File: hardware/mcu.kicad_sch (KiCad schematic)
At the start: 25 parts, among them SW1 SW_Push, SW4 SW_Push, U1 STM32L072RBTx

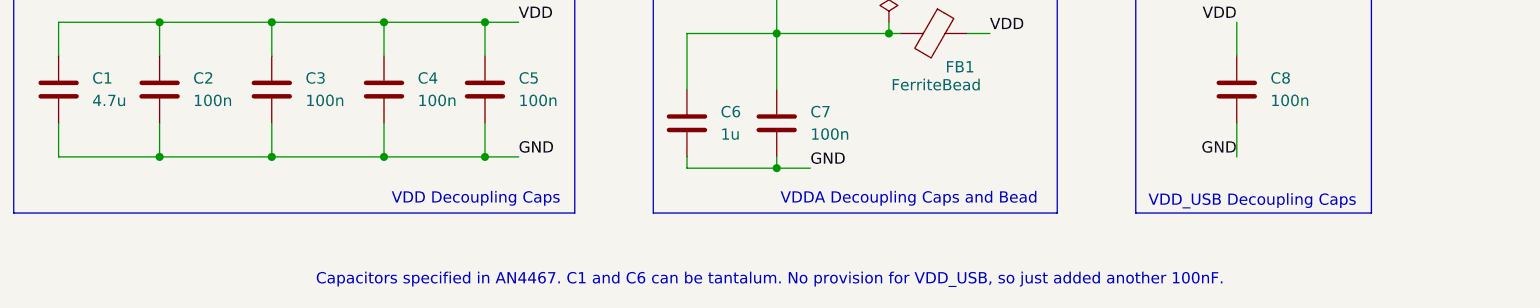
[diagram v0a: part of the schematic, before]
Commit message: [Hardware] Component changes.
* Swap op-amp to similar and cheaper OPA504
* Remove note about tantalum caps (per conversation w Alexa) and plan to replace in BOM with ceramic
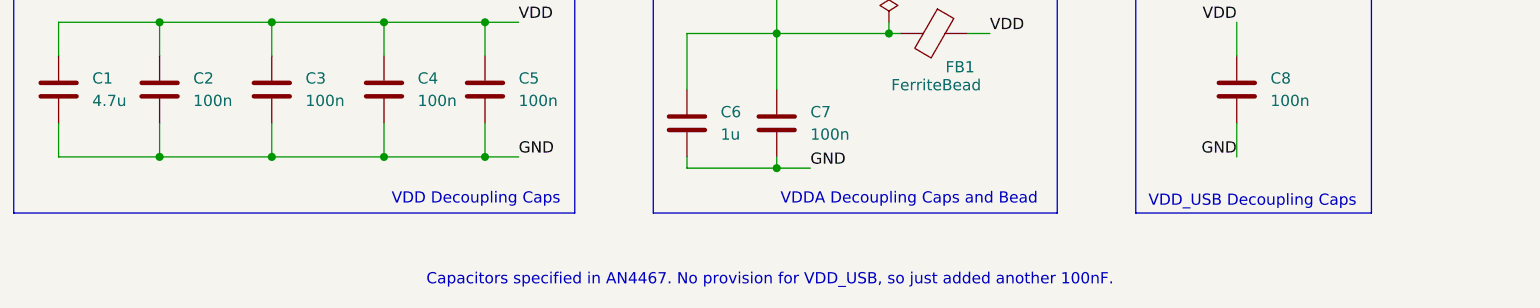
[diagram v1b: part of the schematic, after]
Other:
- note added: "Capacitors specified in AN4467. No provision for VDD_USB, so just added another 100nF."
- note removed: "Capacitors specified in AN4467. C1 and C6 can be tantalum. No provision for VDD_USB, so just added another 100nF."
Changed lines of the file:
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@@
 		)
 	)
-	(text "Capacitors specified in AN4467. C1 and C6 can be tantalum. No provision for VDD_USB, so just added another 100nF."
+	(text "Capacitors specified in AN4467. No provision for VDD_USB, so just added another 100nF."
 		(exclude_from_sim no)
 		(at 102.108 191.77 0)

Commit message: Change many passives to 0402 and assign part numbers
Incorporate 0402 parts where possible
Assign Manufacturer Part Numbers to parts where possible
Update layout for the new passive sizes
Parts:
- C1: footprint Capacitor_SMD:C_0603_1608Metric_Pad1.08x0.95mm_HandSolder -> Capacitor_SMD:C_0402_1005Metric; MPN (none) -> CL05A475MP5NRNC
- C2, C3, C4, C5, C7, C8: footprint Capacitor_SMD:C_0603_1608Metric_Pad1.08x0.95mm_HandSolder -> Capacitor_SMD:C_0402_1005Metric; MPN (none) -> CL05A104KA5NNNC
- C6: MPN (none) -> CL05A105KO5NNNC
- FB1: MPN (none) -> 742792662
- R1, R3, R6, R7: footprint Resistor_SMD:R_0603_1608Metric_Pad0.98x0.95mm_HandSolder -> Resistor_SMD:R_0402_1005Metric; MPN (none) -> RC0402FR-0710KL
- R25, R26: footprint Resistor_SMD:R_0603_1608Metric_Pad0.98x0.95mm_HandSolder -> Resistor_SMD:R_0402_1005Metric; MPN (none) -> RC0402FR-07100KL
- U1: MPN (none) -> STM32L072RBT6

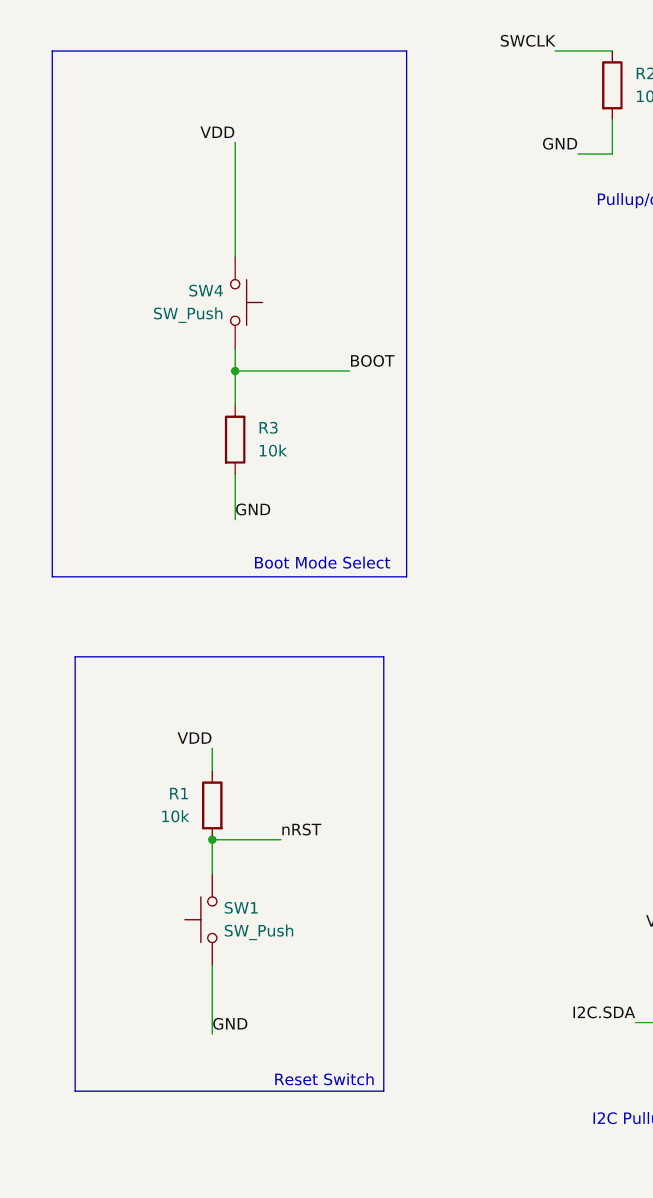
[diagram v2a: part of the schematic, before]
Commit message: Replace buttons with jumper pads
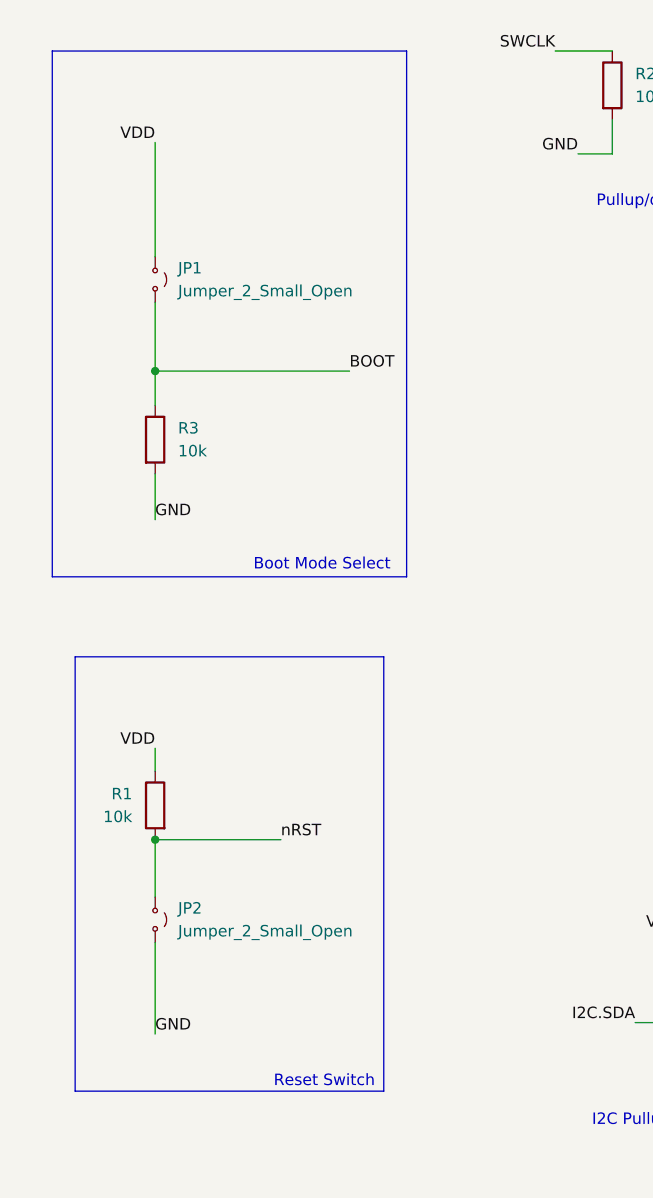
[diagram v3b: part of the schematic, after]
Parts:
- removed SW1, SW4: SW_Push, Button_Switch_SMD:SW_Push_1P1T_NO_6x6mm_H9.5mm, symbol Switch:SW_Push
- added JP1, JP2: Jumper_2_Small_Open, Jumper:SolderJumper-2_P1.3mm_Open_RoundedPad1.0x1.5mm, symbol Jumper:Jumper_2_Small_Open
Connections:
- net BOOT: now also JP1.2 (B)
- net GND: now also JP2.2 (B)
- net VDD: now also JP1.1 (A)
- net nRST: now also JP2.1 (A)
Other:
- moved on the sheet: R1, R3

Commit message: Remove status LEDs
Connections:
- net STAT_LED0: no longer names the net of U1.41 (PA8)
- net STAT_LED1: no longer names the net of U1.42 (PA9)
- no-connect marks 18 -> 20
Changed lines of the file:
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@@
+	)
+	(no_connect
+		(at 157.48 66.04)
 	)
 	(no_connect
@@
 	(no_connect
 		(at 157.48 116.84)
+	)
+	(no_connect
+		(at 157.48 68.58)
 	)
 	(no_connect
@@
 	)
 	(bus_entry
-		(at 222.25 146.05)
-		(size -2.54 2.54)
-		(stroke
-			(width 0)
-			(type default)
-		)
-	)
-	(bus_entry
 		(at 217.17 82.55)
 		(size 2.54 -2.54)
@@
 	)
 	(bus_entry
-		(at 222.25 143.51)
-		(size -2.54 2.54)
-		(stroke
-			(width 0)
-			(type default)
-		)
-	)
-	(bus_entry
 		(at 217.17 77.47)
 		(size 2.54 -2.54)
@@
 	(wire
 		(pts
-			(xy 209.55 146.05) (xy 219.71 146.05)
-		)
-		(stroke
-			(width 0)
-			(type default)
-		)
-	)
-	(wire
-		(pts
 			(xy 104.14 31.75) (xy 104.14 35.56)
 		)
@@
 	(wire
 		(pts
-			(xy 209.55 148.59) (xy 219.71 148.59)
-		)
-		(stroke
-			(width 0)
-			(type default)
-		)
-	)
-	(wire
-		(pts
 			(xy 228.6 118.11) (xy 237.49 118.11)
 		)
@@
 		)
 	)
-	(bus
-		(pts
-			(xy 240.03 143.51) (xy 222.25 143.51)
-		)
-		(stroke
-			(width 0)
-			(type default)
-		)
-	)
 	(wire
 		(pts
@@
 		)
 	)
-	(bus
-		(pts
-			(xy 222.25 143.51) (xy 222.25 146.05)
-		)
-		(stroke
-			(width 0)
-			(type default)
-		)
-	)
 	(wire
 		(pts
@@
 	(wire
 		(pts
-			(xy 157.48 66.04) (xy 160.02 66.04)
-		)
-		(stroke
-			(width 0)
-			(type default)
-		)
-	)
-	(wire
-		(pts
 			(xy 210.82 72.39) (xy 217.17 72.39)
 		)
@@
 		(pts
 			(xy 234.95 123.19) (xy 237.49 123.19)
-		)
-		(stroke
-			(width 0)
-			(type default)
-		)
-	)
-	(wire
-		(pts
-			(xy 157.48 68.58) (xy 160.02 68.58)
 		)
 		(stroke
@@
 		)
 	)
-	(label "STAT_LED0"
-		(at 160.02 66.04 0)
-		(fields_autoplaced yes)
-		(effects
-			(font
-				(size 1.27 1.27)
-			)
-			(justify left bottom)
-		)
-	)
 	(label "nRST"
 		(at 217.17 30.48 180)
@@
 		)
 	)
-	(label "STAT_LED[0..1]"
-		(at 223.52 143.51 0)
-		(fields_autoplaced yes)
-		(effects
-			(font
-				(size 1.27 1.27)
-			)
-			(justify left bottom)
-		)
-	)
 	(label "nRST"
 		(at 119.38 45.72 180)
@@
 		)
 	)
-	(label "STAT_LED1"
-		(at 209.55 148.59 0)
-		(fields_autoplaced yes)
-		(effects
-			(font
-				(size 1.27 1.27)
-			)
-			(justify left bottom)
-		)
-	)
 	(label "LED6"
 		(at 210.82 64.77 0)
@@
 		)
 	)
-	(label "STAT_LED0"
-		(at 209.55 146.05 0)
-		(fields_autoplaced yes)
-		(effects
-			(font
-				(size 1.27 1.27)
-			)
-			(justify left bottom)
-		)
-	)
 	(label "LED8"
 		(at 113.03 88.9 0)
@@
 	(label "LED9"
 		(at 113.03 91.44 0)
-		(fields_autoplaced yes)
-		(effects
-			(font
-				(size 1.27 1.27)
-			)
-			(justify left bottom)
-		)
-	)
-	(label "STAT_LED1"
-		(at 160.02 68.58 0)
 		(fields_autoplaced yes)
 		(effects
@@
 		(fields_autoplaced yes)
 		(effects
-			(font
-				(size 1.27 1.27)
-			)
-			(justify left)
-		)
-	)
-	(hierarchical_label "STAT_LED[0..1]"
-		(shape output)
-		(at 240.03 143.51 0)
-		(fields_autoplaced yes)
-		(effects
